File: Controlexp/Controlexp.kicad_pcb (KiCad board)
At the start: 2 copper layers, 100.3 x 100.3 mm, 26 parts, among them J1 SMA_CONNECTOR, J4 530470510, J5 Power Connector, J6 Pressure sensor, J7 POWER PROBE, U2 RFM95W, U3 TPS62162DSG, U4 BME680, U5 XIAO-nRF52840-DIP

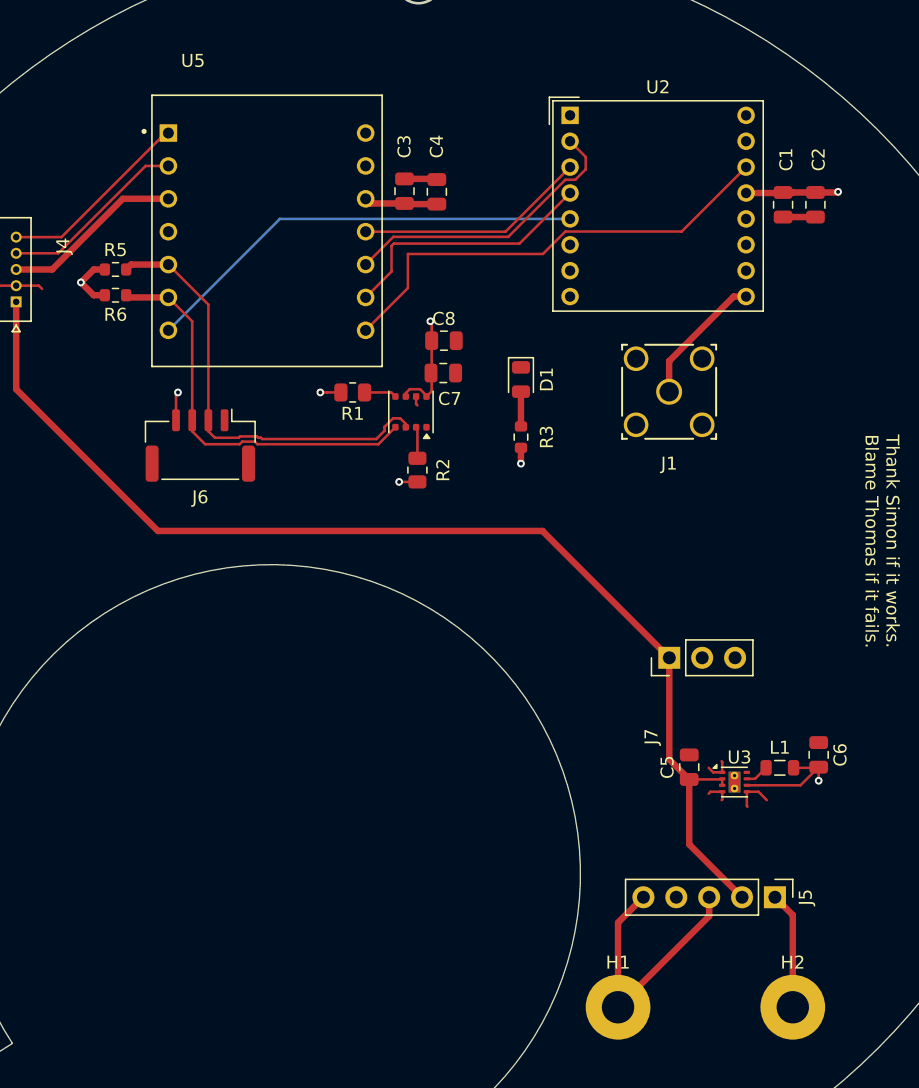
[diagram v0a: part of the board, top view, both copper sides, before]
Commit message: lil fixes + sma gnd fix.
Added gnd stitching and connected the sma gnd. and fixed some connections
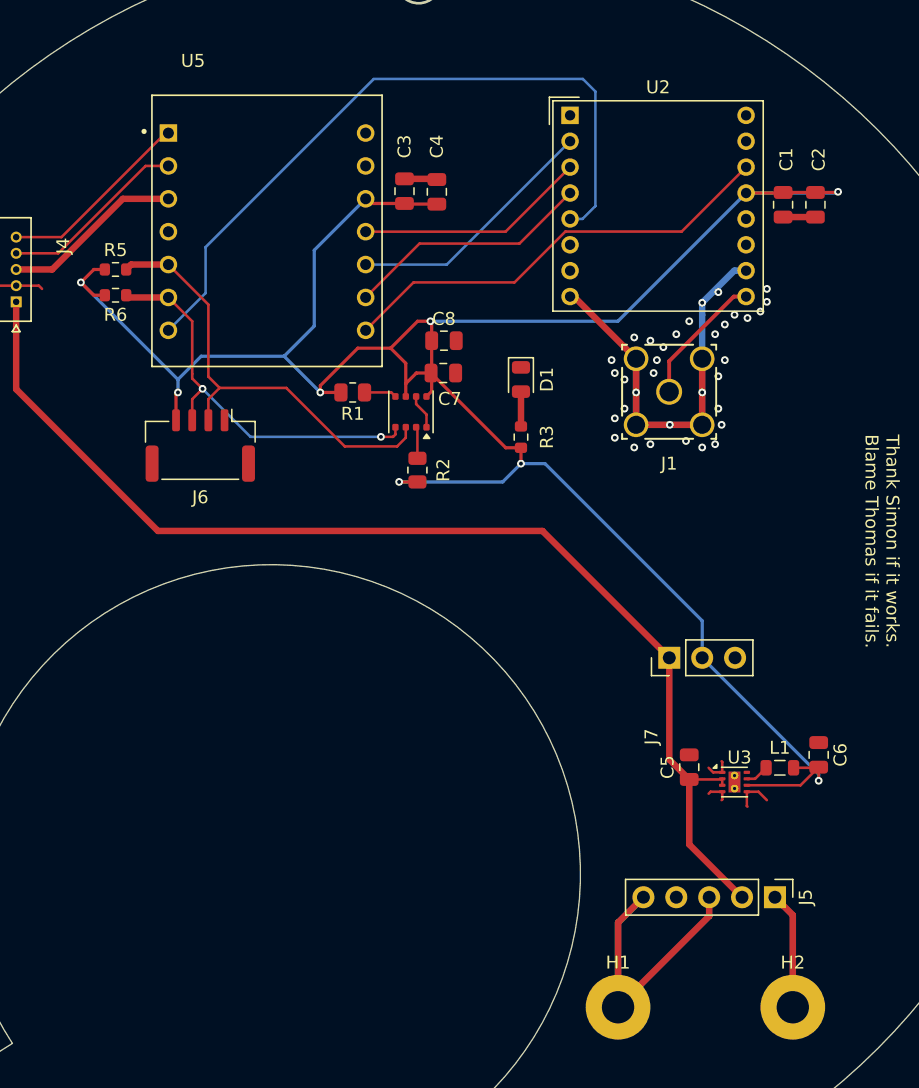
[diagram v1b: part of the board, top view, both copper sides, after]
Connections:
- J1 pad 2: (no net) -> GND
- J1 pad 3: (no net) -> GND
- J1 pad 4: (no net) -> GND
- J1 pad 5: (no net) -> GND
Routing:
- net +3.3V: track 41.9 -> 186.7 mm
- net GND: track 37.5 -> 106.7 mm, vias 0 -> 34
- net /NSS: track 34.6 -> 54.7 mm
- net /MAIN: track 9.07 -> 18.1 mm
- net /MISO: track 22.7 -> 19.7 mm
- net /INT: track 36.2 -> 34.6 mm
- net /SCK: track 20.3 -> 19.1 mm
- net /SCL: vias 0 -> 2
- added copper zone on B.Cu, net GND
- removed copper zone on B.Cu, net +3.3V

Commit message: fresh board
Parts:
- removed C7: 0.1uF, Capacitor_SMD:C_0805_2012Metric
- removed C8: 10uF, Capacitor_SMD:C_0805_2012Metric
- removed H1: GND, MountingHole:MountingHole_2.5mm_Pad
- removed H2: 12V, MountingHole:MountingHole_2.5mm_Pad
- removed R1, R2: 10k, Resistor_SMD:R_0805_2012Metric
- removed U4: BME680, Package_LGA:Bosch_LGA-8_3x3mm_P0.8mm_ClockwisePinNumbering
- added C10: 220 uF, Capacitor_SMD:C_0805_2012Metric, F.Cu at (141.9, 47.2)
- added C11: 10uF, 25V, Capacitor_SMD:C_0805_2012Metric, F.Cu at (141.4, 50.3)
- added C12: 22uF, 10V, Capacitor_SMD:C_0805_2012Metric, F.Cu at (148.1, 45.7)
- added C13: 100nF, Capacitor_SMD:C_0805_2012Metric, F.Cu at (135.5, 73.9)
- added C14: 100nF, Capacitor_SMD:C_0805_2012Metric, F.Cu at (142.0, 71.3)
- added C9: 220 uF, Capacitor_SMD:C_0805_2012Metric, F.Cu at (169.0, 77.5)
- added D2: SS34, SS34:DIOM7959X265N, F.Cu at (101.5, 69.5)
- added J10: Extra sensor TOP, Connector_JST:JST_GH_BM04B-GHS-TBT_1x04-1MP_P1.25mm_Vertical, F.Cu at (109.5, 76.9)
- added J11: Extra sensor BOTTOM, Connector_JST:JST_GH_BM04B-GHS-TBT_1x04-1MP_P1.25mm_Vertical, B.Cu at (128.9, 78.3)
- added J2: Conn_01x02, 250-202:P-250-202, B.Cu at (175.4, 67.5)
- added J8: LED, Connector_JST:JST_GH_BM04B-GHS-TBT_1x04-1MP_P1.25mm_Vertical, F.Cu at (153.9, 46.9)
- added J9: PWRCONN, Connector_JST:JST_GH_BM03B-GHS-TBT_1x03-1MP_P1.25mm_Vertical, F.Cu at (179.7, 87.2)
- added JBUTT1: Conn_01x02, Connector_PinHeader_2.54mm:PinHeader_1x02_P2.54mm_Vertical, F.Cu at (177.6, 92.8)
- added L2: 2.2uH, Inductor_SMD:L_0805_2012Metric, F.Cu at (145.3, 46.7)
- added REF**: SolderJumper-2_P1.3mm_Open_TrianglePad1.0x1.5mm, Jumper:SolderJumper-2_P1.3mm_Open_TrianglePad1.0x1.5mm, F.Cu at (176.6, 81.5)
- added U1: XIAO-ESP32-S3-Plus-SMD, New_XIAO_Series_Footprints:XIAO-ESP32-S3-Plus-SMD, F.Cu at (130.8, 62.1)
- added U6: SN74LVC1T45DBV, Package_TO_SOT_SMD:SOT-23-6, F.Cu at (144.6, 54.0)
- added U7: BMP388, BMP388:XDCR_BMP388, F.Cu at (139.4, 75.1)
- J1: value SMA_CONNECTOR -> Conn_Coaxial_Small; footprint SMASMA2:CONN_RF2-04A-T-00-50-G_ADM -> SMAv2:CONN_RF2-04A-T-00-50-G_ADM
- J4: moved to B.Cu
- J7: value POWER PROBE -> ToF sensor; footprint Connector_PinHeader_2.54mm:PinHeader_1x03_P2.54mm_Vertical -> Connector_JST:JST_GH_BM04B-GHS-TBT_1x04-1MP_P1.25mm_Vertical
- U5: value XIAO-nRF52840-DIP -> TPS62163DSG; footprint MCU_SEED:MODULE_113991054 -> Package_SON:WSON-8-1EP_2x2mm_P0.5mm_EP0.9x1.6mm_ThermalVias
- moved J7 61.7 mm to (113.2, 55.4), turned to 180 degrees
- moved C5 31.1 mm to (173.3, 74.5)
- moved C6 31.1 mm to (183.3, 73.6)
- moved L1 31.1 mm to (180.3, 74.6)
- moved U3 31.1 mm to (176.8, 75.7)
- moved J5 24.3 mm to (171.1, 89.3)
- moved U5 20.0 mm to (145.3, 49.9)
- moved J4 5.26 mm to (108.5, 62.5), turned to 90 degrees
- moved J6 4.11 mm to (120.1, 78.3), turned to 90 degrees
- moved D1 2.27 mm to (147.7, 71.6), turned to 0 degrees
- moved C4 1.85 mm to (144.3, 58.7)
- moved C3 1.34 mm to (141.3, 58.7)
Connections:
- J4 pad 1: +12V -> /PWM
- J4 pad 3: /PWM -> /DIR
- J4 pad 4: /DIR -> /FEEDBACK
- J4 pad 5: /FEEDBACK -> +12V
- J5 pad 1: /MAIN -> +12V
- J5 pad 4: +3V3 -> +3.3V
- J6 pad 2: /SDA -> /BMPSDA
- J6 pad 3: /SCL -> /BMPSCL
- J7 pad 1: +12V -> GND
- J7 pad 2: +3.3V -> /BMPSDA
- J7 pad 3: GND -> /BMPSCL
- R5 pad 1: /SDA -> /BMPSDA
- R6 pad 1: /SCL -> /BMPSCL
- U5 pad 1: /FEEDBACK -> GND
- U5 pad 2: /DIR -> +12V
- U5 pad 3: /PWM -> +12V
- U5 pad 4: /PWR_SWITCH -> GND
- U5 pad 5: /SDA -> GND
- U5 pad 6: /SCL -> +5V
- U5 pad 7: /NSS -> Net-(U5-SW)
- U5 pad 8: /INT -> unconnected-(U5-PG-Pad8)
- U5 pad 9: /SCK -> GND
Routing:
- net +12V: track 89.7 -> 215.2 mm, vias 0 -> 2
- net /BMPSCL: track 0.00 -> 80.1 mm, vias 0 -> 4
- net +3.3V: track 186.7 -> 261.9 mm, vias 8 -> 12
- net /BMPSDA: track 0.00 -> 73.8 mm, vias 0 -> 3
- net /SDA: track 34.8 -> 0.00 mm
- net /SCL: track 31.3 -> 0.00 mm, vias 2 -> 0
- net GND: track 106.7 -> 133.9 mm, vias 34 -> 64
- net /LEDSERIAL: track 0.00 -> 21.6 mm, vias 0 -> 2
- net /MAIN: track 18.1 -> 0.00 mm
- net +5V: track 0.00 -> 15.9 mm
- net /DIN: track 0.00 -> 11.6 mm
- net Net-(U5-SW): track 0.00 -> 4.63 mm
- net Net-(U7-VDD): track 0.00 -> 4.23 mm
- net /NSS: track 54.7 -> 58.7 mm, vias 0 -> 1
- net /PWM: track 14.0 -> 17.3 mm
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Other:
- board size 100.3 x 100.3 mm -> 98.7 x 59.5 mm
- board text added: "12V"
- board text added: "3V3"
- board text added: "By Simon Hajduk and Thomas Gust"
- board text added: "GND"
- board text removed: "FEB 3, 2026"
- board text removed: "Thank Simon if it works. Blame Thomas if it fails."
- board text removed: "Triton Robotics Float Controller REV2"
